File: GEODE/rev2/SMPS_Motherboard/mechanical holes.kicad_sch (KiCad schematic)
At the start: 30 parts

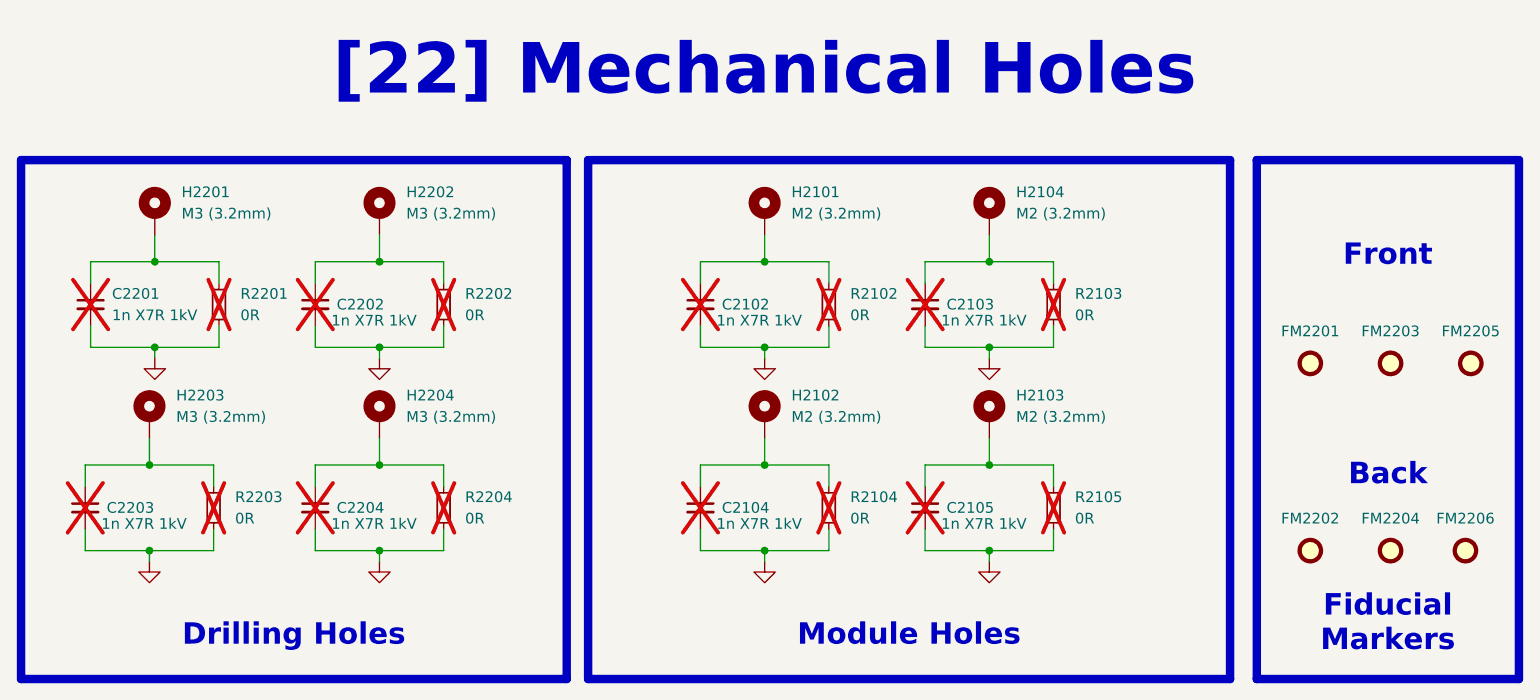
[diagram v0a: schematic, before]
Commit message: changed connectors, removed can, added fuse, disconnected EXTVCC in power generation
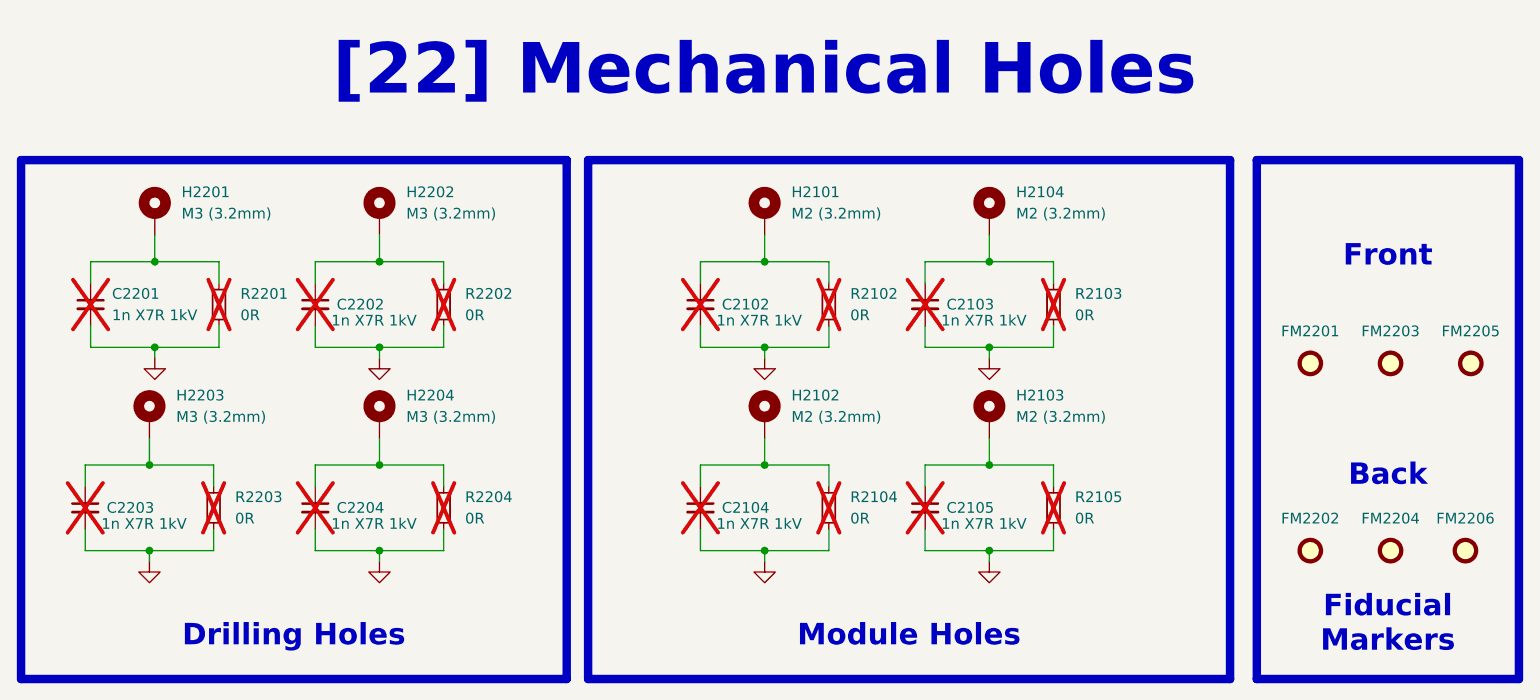
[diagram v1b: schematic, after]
